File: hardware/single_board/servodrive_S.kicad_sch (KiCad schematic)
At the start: 0 parts

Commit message: Board S schematic: drawn as a person would draw it, and on the page
The sheets were a grid of parts with a stub and a label on every pin.
tools/schdraw.py now draws a netlist from a hand-written layout: parts
placed and turned, wires between the pins that belong together, T-joins
split with a junction dot, ground and supply symbols on power pins, labels
only where a signal leaves its block. tools/schlayout_s.py is board S's
five sheets: signal left to right, supplies up, ground down, each part's
support parts at the pin they serve, dashed frames and notes. The header
pins and the notes follow the netlist, so a pin-map change redraws itself.

The drawing cannot change the circuit: every sheet is checked against
schematic_s's netlist before it is written, and `schdraw.py --check s`
compares KiCad's own netlist export net by net. It matches; ERC is 0 at
every severity; PCB parity is unchanged (the same 219 reports as before).

Found on the way: a symbol's instance path must be /<root>/<sheet>. With
the root left out, as schematic.py writes it, KiCad joins labelled nets
but silently drops every net that is only wire -- the old sheets labelled
every pin, so it never showed. Board A's generator is unchanged.

single.html: an SCH tab in the viewer (sch.js) -- the sheets as KiCad
plots them, a sheet list, drag to pan, scroll to zoom, a PDF of the lot.
tools/regen.py plots them into img/sch/s/ (--sch for that alone).

Co-Authored-By: Claude Opus 5.5 (1M context) <noreply@anthropic.com>
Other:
- note added: "Board A plus the minimum of board B. 48 V max. XT30 bus input, TVS and cans, two LMR38010 rails, USB-C, RS-485 relay on two SH 6, expansion header."
- note added: "XT30 bus input, SMDJ54A, 2x 100 uF polymer, bus divider, 2x LMR38010: 12 V gate rail (GATE_OFF stops it), 5 V logic"
- note removed: "Board A plus the minimum of board B. 48 V max. Bus pads, TVS and cans, two LMR38010 rails, USB-C, RS-485 relay on two SH 6, expansion header."
- note removed: "Bus pads, SMDJ54A, 2x 100 uF polymer, bus divider, 2x LMR38010: 12 V gate rail (GATE_OFF kills it), 5 V logic"
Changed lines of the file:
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@@
 	(title_block (title "servodrive — board S, single board") (date "2026-09-07") (rev "A")
 		(company "Sequoia Hope Alexander")
-		(comment 1 "Sheet skeleton generated by tools/gen_boards.py")
-		(comment 2 "Capture is manual from here. See ../../spec.html")
+		(comment 1 "Sheets drawn by tools/schlayout_s.py from the netlist in tools/schematic_s.py")
+		(comment 2 "See ../../single.html")
 		(comment 3 "CERN-OHL-P"))
 	(sheet (at 25.0 35.0) (size 60 18)
@@
 		(instances (project "servodrive_S" (path "/" (page "5"))))
 	)
-	(text "Bus pads, SMDJ54A, 2x 100 uF polymer, bus divider,\n2x LMR38010: 12 V gate rail (GATE_OFF kills it), 5 V logic" (exclude_from_sim no) (at 26.5 112.0 0)
+	(text "XT30 bus input, SMDJ54A, 2x 100 uF polymer, bus divider,\n2x LMR38010: 12 V gate rail (GATE_OFF stops it), 5 V logic" (exclude_from_sim no) (at 26.5 112.0 0)
 		(effects (font (size 1.0 1.0)) (justify left top)))
 	(sheet (at 25.0 131.0) (size 60 18)
@@
 	(text "USB-C (data + 5 V), RS-485 relay on two SH 6, expansion header,\nRGB LED, BOOTSEL, test pads" (exclude_from_sim no) (at 26.5 136.0 0)
 		(effects (font (size 1.0 1.0)) (justify left top)))
-	(text "Board A plus the minimum of board B. 48 V max. Bus pads, TVS and cans, two LMR38010 rails, USB-C, RS-485 relay on two SH 6, expansion header." (exclude_from_sim no) (at 25 25 0)
+	(text "Board A plus the minimum of board B. 48 V max. XT30 bus input, TVS and cans, two LMR38010 rails, USB-C, RS-485 relay on two SH 6, expansion header." (exclude_from_sim no) (at 25 25 0)
 		(effects (font (size 1.27 1.27) (bold yes)) (justify left top)))
 	(sheet_instances

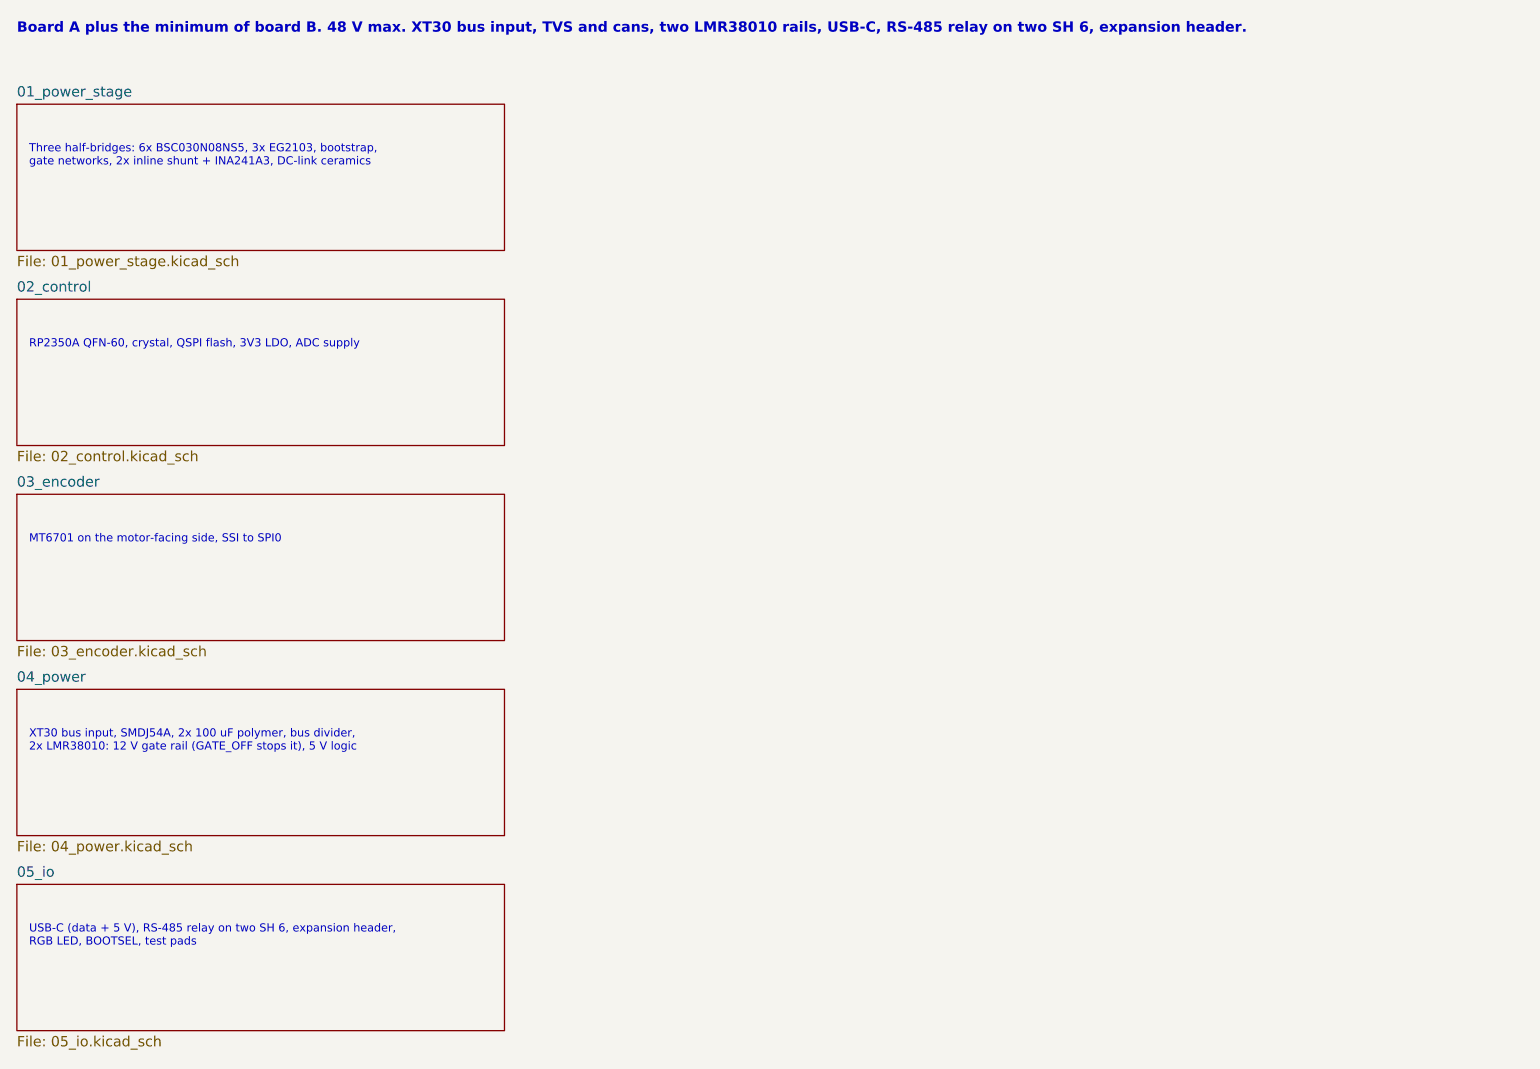
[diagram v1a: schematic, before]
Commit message: Board S schematic on three sheets: bridge + CPU, power, encoder + IO
Asked for fewer pages: the power bridge goes with the CPU that drives it
(A2), the encoder with the rest of the IO (A3); the supplies keep their
sheet. schematic_s.SHEET_OF maps the parts' sheet names (board A keeps its
own), and schdraw.Sheet.origin() lets a sheet place layouts written in their
own coordinates side by side. HIN/LIN and the other CPU-to-bridge nets are
now local labels on one sheet. The notes say which sheet a part is on.

KiCad's netlist matches schematic_s.nets(); ERC 0. The board is linked to
the netlist by reference, so the PCB is untouched.

Co-Authored-By: Claude Opus 5.5 (1M context) <noreply@anthropic.com>
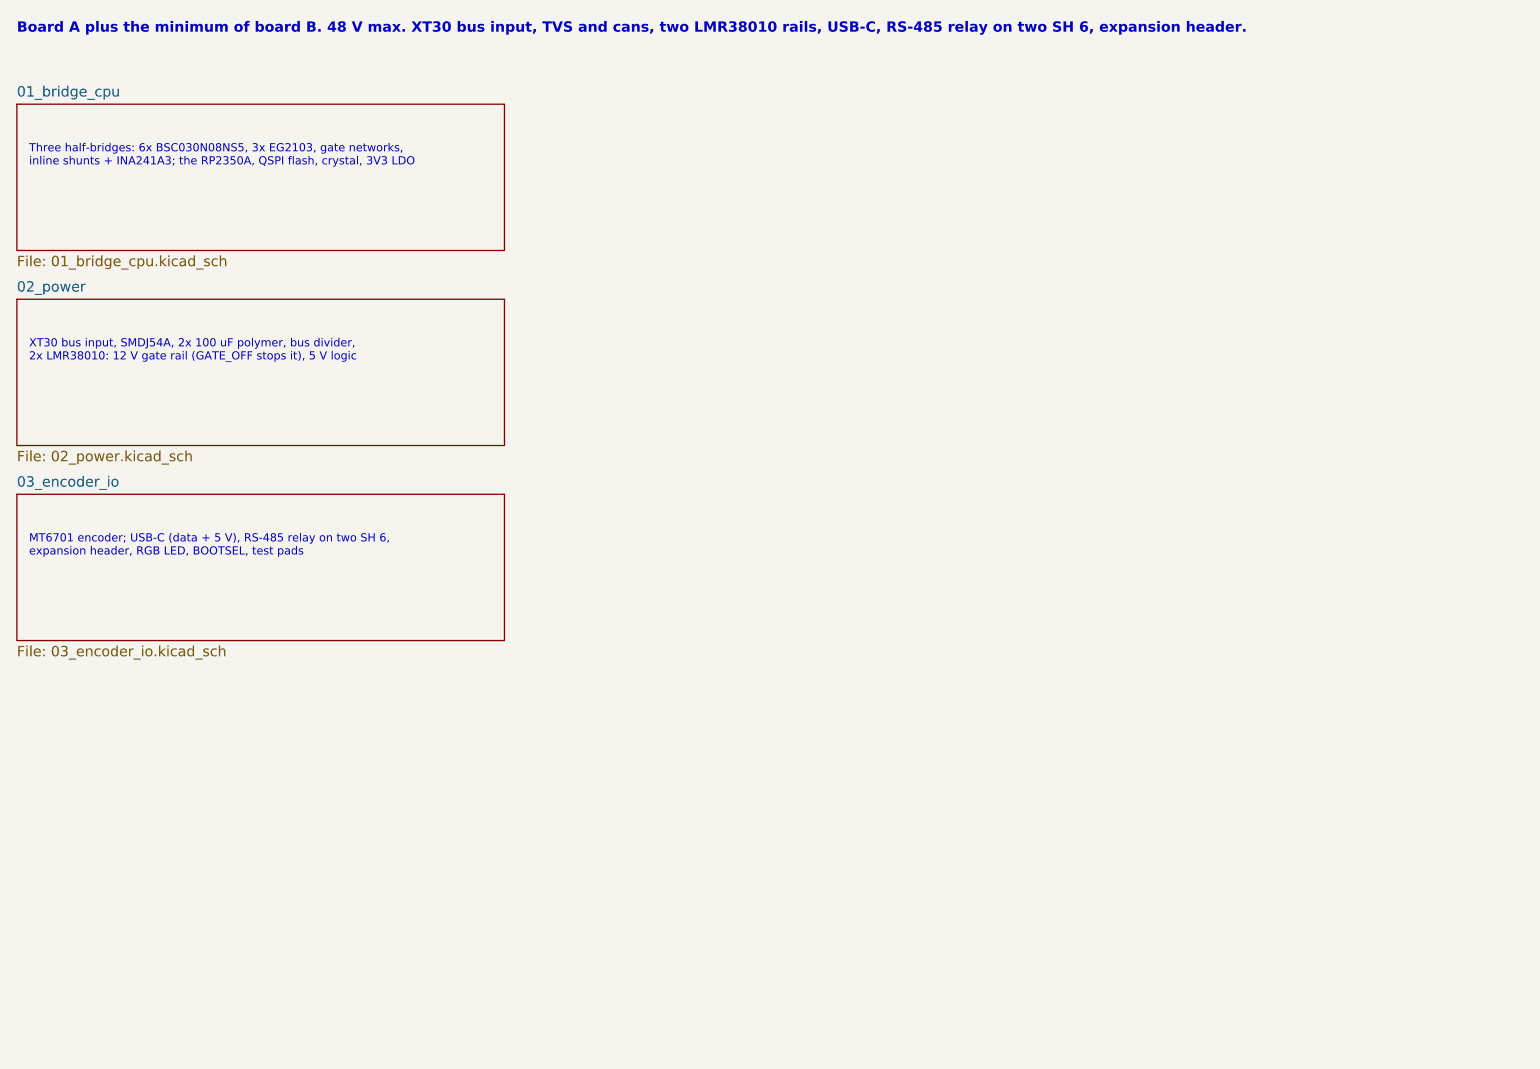
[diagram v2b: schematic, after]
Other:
- removed sheet 01_power_stage
- removed sheet 02_control
- removed sheet 03_encoder
- removed sheet 04_power
- removed sheet 05_io
- added sheet 01_bridge_cpu (01_bridge_cpu.kicad_sch)
- added sheet 02_power (02_power.kicad_sch)
- added sheet 03_encoder_io (03_encoder_io.kicad_sch)
- note added: "MT6701 encoder; USB-C (data + 5 V), RS-485 relay on two SH 6, expansion header, RGB LED, BOOTSEL, test pads"
- note added: "Three half-bridges: 6x BSC030N08NS5, 3x EG2103, gate networks, inline shunts + INA241A3; the RP2350A, QSPI flash, crystal, 3V3 LDO"
- note removed: "MT6701 on the motor-facing side, SSI to SPI0"
- note removed: "RP2350A QFN-60, crystal, QSPI flash, 3V3 LDO, ADC supply"
- note removed: "Three half-bridges: 6x BSC030N08NS5, 3x EG2103, bootstrap, gate networks, 2x inline shunt + INA241A3, DC-link ceramics"
- note removed: "USB-C (data + 5 V), RS-485 relay on two SH 6, expansion header, RGB LED, BOOTSEL, test pads"
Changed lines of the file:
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@@
 		(stroke (width 0.1524) (type solid))
 		(fill (color 0 0 0 0.0000))
-		(property "Sheetname" "01_power_stage" (at 25.0 34.21 0)
+		(property "Sheetname" "01_bridge_cpu" (at 25.0 34.21 0)
 			(effects (font (size 1.27 1.27)) (justify left bottom)))
-		(property "Sheetfile" "01_power_stage.kicad_sch" (at 25.0 53.6 0)
+		(property "Sheetfile" "01_bridge_cpu.kicad_sch" (at 25.0 53.6 0)
 			(effects (font (size 1.27 1.27)) (justify left top)))
 		(instances (project "servodrive_S" (path "/" (page "2"))))
 	)
-	(text "Three half-bridges: 6x BSC030N08NS5, 3x EG2103, bootstrap,\ngate networks, 2x inline shunt + INA241A3, DC-link ceramics" (exclude_from_sim no) (at 26.5 40.0 0)
+	(text "Three half-bridges: 6x BSC030N08NS5, 3x EG2103, gate networks,\ninline shunts + INA241A3; the RP2350A, QSPI flash, crystal, 3V3 LDO" (exclude_from_sim no) (at 26.5 40.0 0)
 		(effects (font (size 1.0 1.0)) (justify left top)))
 	(sheet (at 25.0 59.0) (size 60 18)
@@
 		(stroke (width 0.1524) (type solid))
 		(fill (color 0 0 0 0.0000))
-		(property "Sheetname" "02_control" (at 25.0 58.21 0)
+		(property "Sheetname" "02_power" (at 25.0 58.21 0)
 			(effects (font (size 1.27 1.27)) (justify left bottom)))
-		(property "Sheetfile" "02_control.kicad_sch" (at 25.0 77.6 0)
+		(property "Sheetfile" "02_power.kicad_sch" (at 25.0 77.6 0)
 			(effects (font (size 1.27 1.27)) (justify left top)))
 		(instances (project "servodrive_S" (path "/" (page "3"))))
 	)
-	(text "RP2350A QFN-60, crystal, QSPI flash, 3V3 LDO, ADC supply" (exclude_from_sim no) (at 26.5 64.0 0)
+	(text "XT30 bus input, SMDJ54A, 2x 100 uF polymer, bus divider,\n2x LMR38010: 12 V gate rail (GATE_OFF stops it), 5 V logic" (exclude_from_sim no) (at 26.5 64.0 0)
 		(effects (font (size 1.0 1.0)) (justify left top)))
 	(sheet (at 25.0 83.0) (size 60 18)
@@
 		(stroke (width 0.1524) (type solid))
 		(fill (color 0 0 0 0.0000))
-		(property "Sheetname" "03_encoder" (at 25.0 82.21 0)
+		(property "Sheetname" "03_encoder_io" (at 25.0 82.21 0)
 			(effects (font (size 1.27 1.27)) (justify left bottom)))
-		(property "Sheetfile" "03_encoder.kicad_sch" (at 25.0 101.6 0)
+		(property "Sheetfile" "03_encoder_io.kicad_sch" (at 25.0 101.6 0)
 			(effects (font (size 1.27 1.27)) (justify left top)))
 		(instances (project "servodrive_S" (path "/" (page "4"))))
 	)
-	(text "MT6701 on the motor-facing side, SSI to SPI0" (exclude_from_sim no) (at 26.5 88.0 0)
-		(effects (font (size 1.0 1.0)) (justify left top)))
-	(sheet (at 25.0 107.0) (size 60 18)
-		(fields_autoplaced yes)
-		(stroke (width 0.1524) (type solid))
-		(fill (color 0 0 0 0.0000))
-		(property "Sheetname" "04_power" (at 25.0 106.21 0)
-			(effects (font (size 1.27 1.27)) (justify left bottom)))
-		(property "Sheetfile" "04_power.kicad_sch" (at 25.0 125.6 0)
-			(effects (font (size 1.27 1.27)) (justify left top)))
-		(instances (project "servodrive_S" (path "/" (page "5"))))
-	)
-	(text "XT30 bus input, SMDJ54A, 2x 100 uF polymer, bus divider,\n2x LMR38010: 12 V gate rail (GATE_OFF stops it), 5 V logic" (exclude_from_sim no) (at 26.5 112.0 0)
-		(effects (font (size 1.0 1.0)) (justify left top)))
-	(sheet (at 25.0 131.0) (size 60 18)
-		(fields_autoplaced yes)
-		(stroke (width 0.1524) (type solid))
-		(fill (color 0 0 0 0.0000))
-		(property "Sheetname" "05_io" (at 25.0 130.21 0)
-			(effects (font (size 1.27 1.27)) (justify left bottom)))
-		(property "Sheetfile" "05_io.kicad_sch" (at 25.0 149.6 0)
-			(effects (font (size 1.27 1.27)) (justify left top)))
-		(instances (project "servodrive_S" (path "/" (page "6"))))
-	)
-	(text "USB-C (data + 5 V), RS-485 relay on two SH 6, expansion header,\nRGB LED, BOOTSEL, test pads" (exclude_from_sim no) (at 26.5 136.0 0)
+	(text "MT6701 encoder; USB-C (data + 5 V), RS-485 relay on two SH 6,\nexpansion header, RGB LED, BOOTSEL, test pads" (exclude_from_sim no) (at 26.5 88.0 0)
 		(effects (font (size 1.0 1.0)) (justify left top)))
 	(text "Board A plus the minimum of board B. 48 V max. XT30 bus input, TVS and cans, two LMR38010 rails, USB-C, RS-485 relay on two SH 6, expansion header." (exclude_from_sim no) (at 25 25 0)
